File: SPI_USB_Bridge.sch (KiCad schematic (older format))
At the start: 31 parts, among them J6 USB A RECEP., Q5 IRLML2502, Q6 IRLML2502, U15 CY7C65634-28LTXC, U9 MAX3421, Y2 12MHz, Y3 12MHz

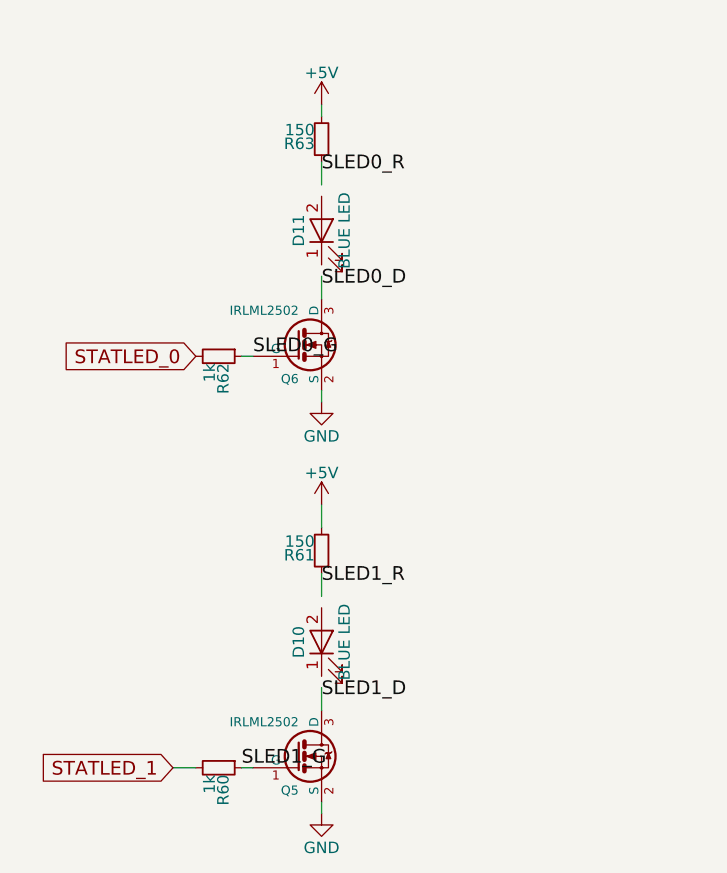
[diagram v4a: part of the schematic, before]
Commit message: Complete BOM. all resistors now 0402
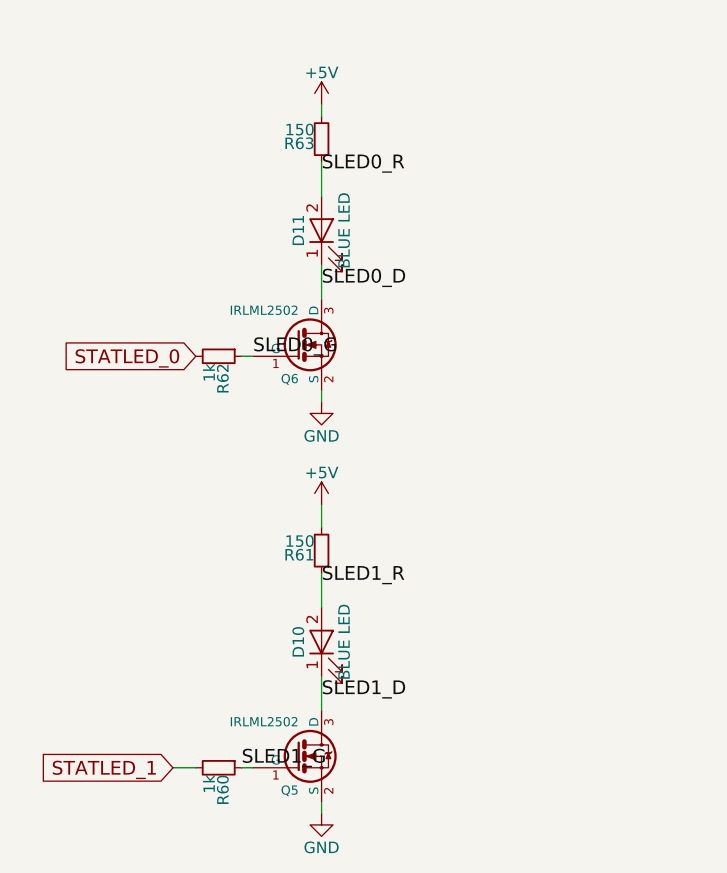
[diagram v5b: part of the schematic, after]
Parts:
- D10, D11: SPN (none) -> VLMB1300-GS08CT-ND; SPR (none) -> Digikey
- NCP1, NCP2: SPN (none) -> NCP361SNT1GOSCT-ND; SPR (none) -> Digikey
- Q5, Q6: SPN (none) -> IRLML2502PBFCT-ND; SPR (none) -> Digikey
- R100, R99: MFR Vishay Dale -> Yageo; MPN CRCW040210K0FKED -> RC0402FR-0710KL; SPN (none) -> 311-10.0KLRTR-ND; SPR (none) -> Digikey
- R101: MFR YAGEO Corporation -> Yageo; SPN (none) -> YAG3206CT-ND; SPR (none) -> Digikey
- R102, R64, R67: footprint Resistors_SMD:R_0603 -> Resistors_SMD:R_0402; MFR Vishay Dale -> Yageo; MPN CRCW060320K0FKEA -> RC0402FR-0720KL; SPN (none) -> 311-20.0KLRCT-ND; SPR (none) -> Digikey
- R60, R62: MFR Vishay Dale -> Yageo; MPN CRCW04021K00FKED -> RC0402FR-071KL; SPN (none) -> 311-1.00KLRCT-ND; SPR (none) -> Digikey
- R61, R63: MFR Vishay Dale -> Yageo; MPN CRCW0402150RFKED -> RC0402FR-07150RL; SPN (none) -> 311-150LRTR-ND; SPR (none) -> Digikey
- R65, R66: MFR Vishay Dale -> Yageo; MPN CRCW040233R0FKED -> RC0402FR-0733RL; SPN (none) -> 311-33.0LRCT-ND; SPR (none) -> Digikey
- U15: SPN (none) -> 428-3154-1-ND; SPR (none) -> Digikey
- U9: SPN (none) -> MAX3421EEHJ+TCT-ND; SPR (none) -> Digikey

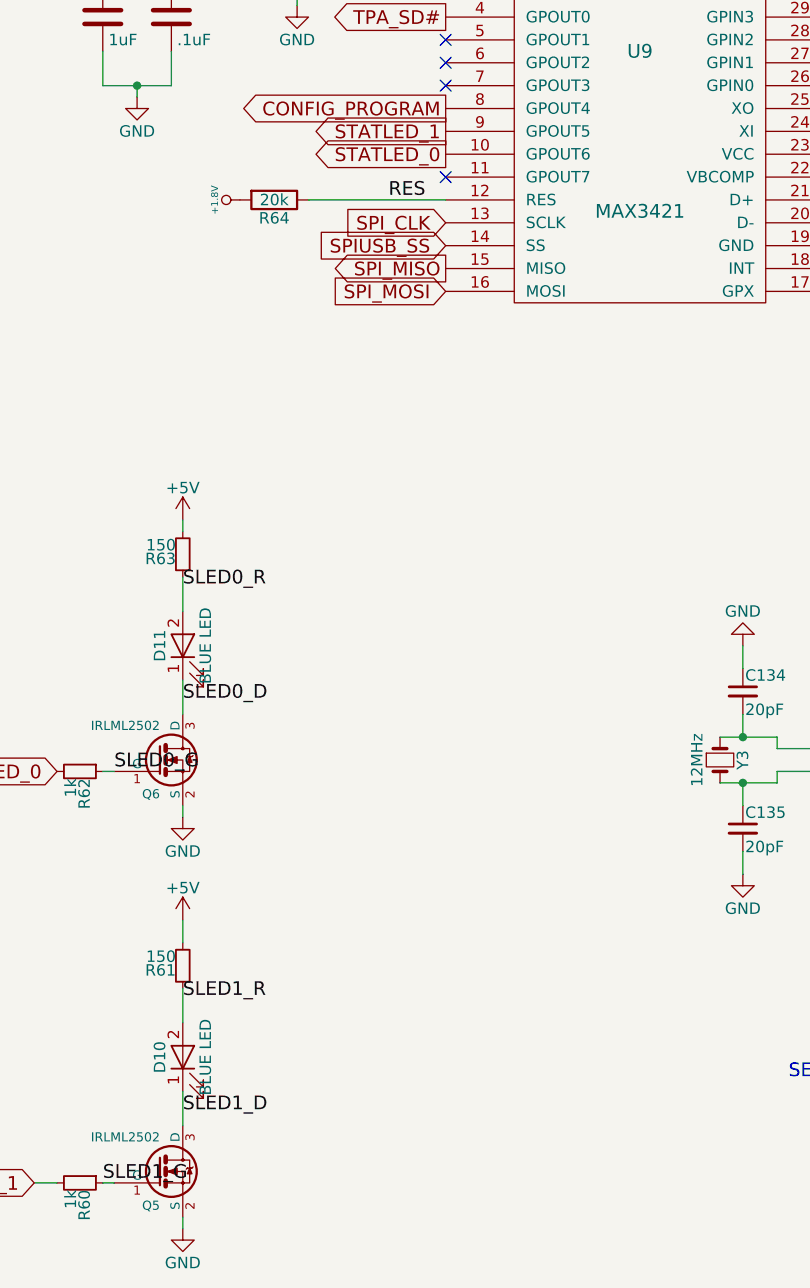
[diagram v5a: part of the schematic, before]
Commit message: added caps to audio
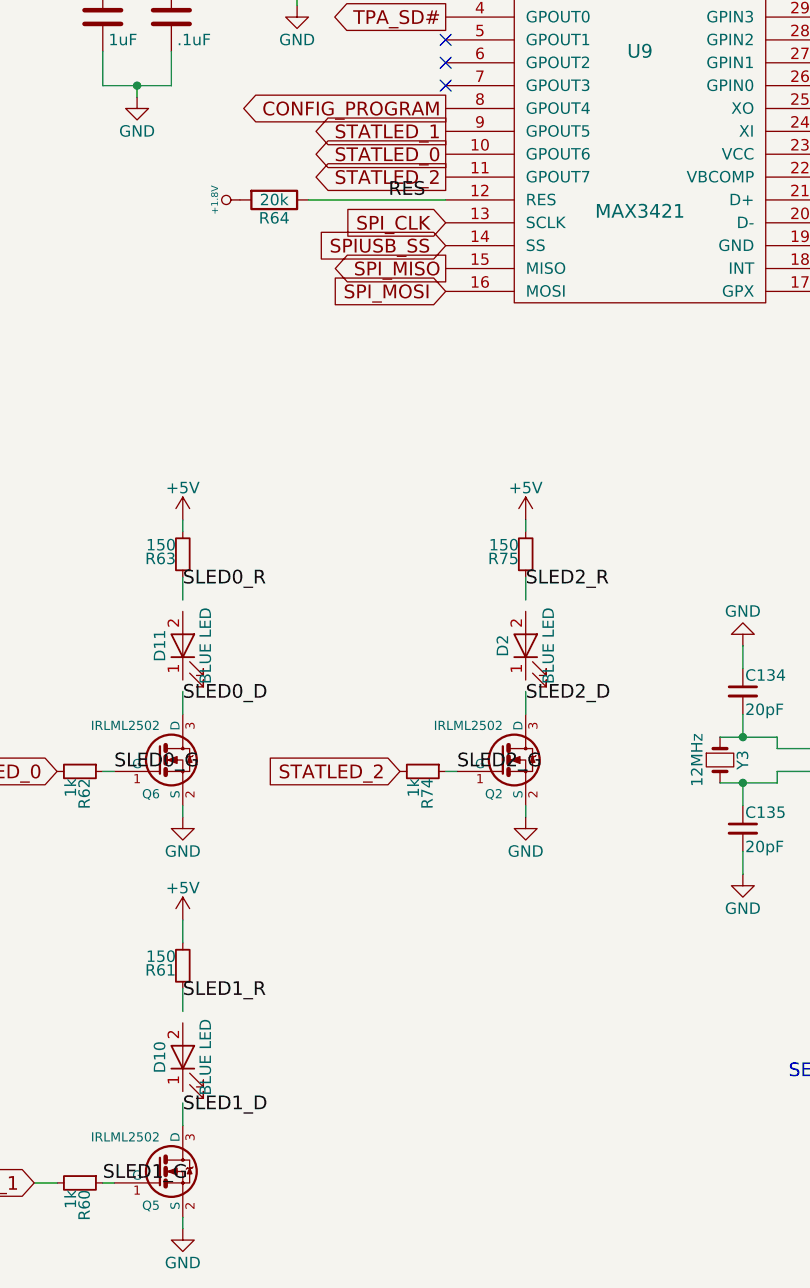
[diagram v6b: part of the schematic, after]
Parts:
- added D2: BLUE LED, LEDs:LED_0603, symbol LED
- added Q2: IRLML2502, TO_SOT_Packages_SMD:SOT-23, symbol IRLML2502
- added R74: 1k, Resistors_SMD:R_0402, symbol R_Small
- added R75: 150, Resistors_SMD:R_0402, symbol R_Small
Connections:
- net labels added: SLED2_D, SLED2_G, SLED2_R, STATLED_2
- wire segments 96 -> 101
- no-connect marks 7 -> 6

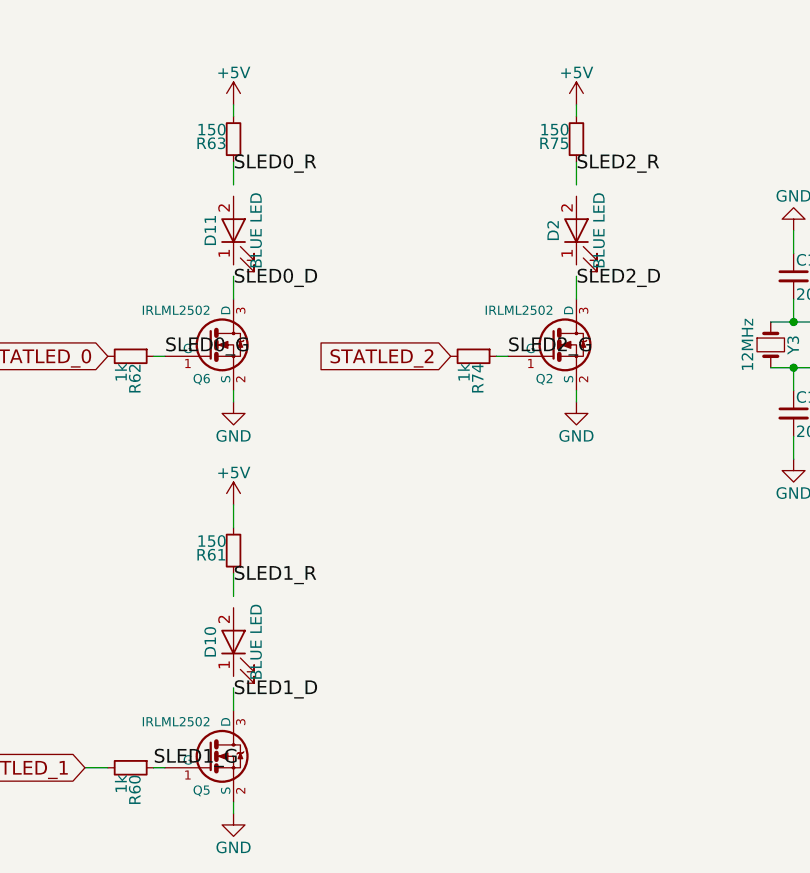
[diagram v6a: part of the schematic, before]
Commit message: about to sed replace all grounds with GND
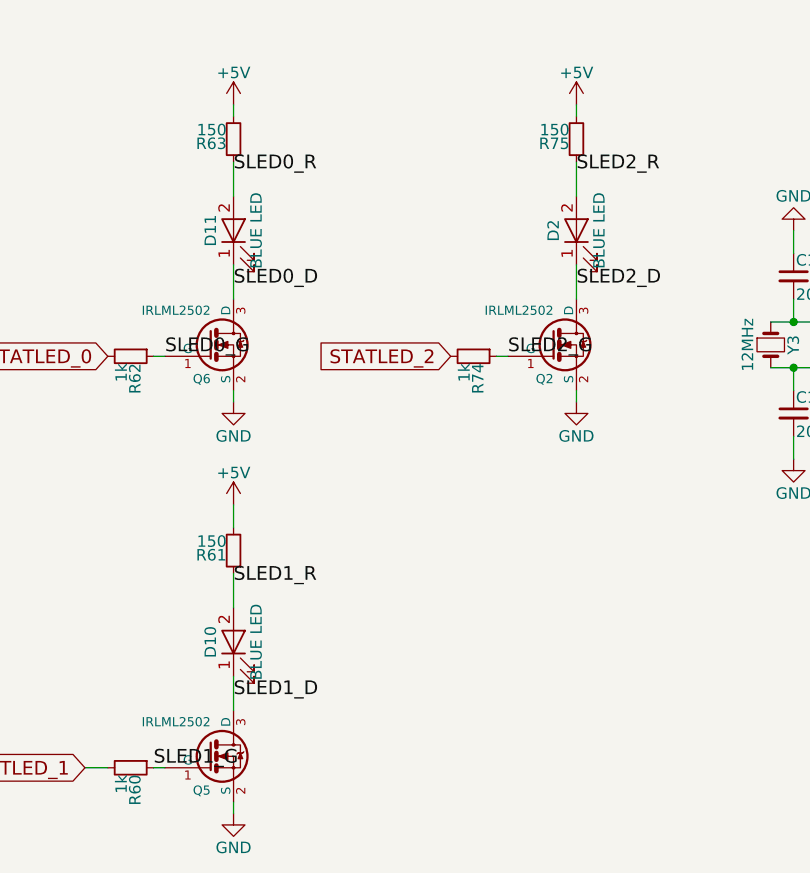
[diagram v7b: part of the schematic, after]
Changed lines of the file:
@@
 LIBS:s70fl01gs
 LIBS:PROpendous-cache
-LIBS:logo
 LIBS:JTAG
 LIBS:Audio-cache
@@
 STATLED_2
 Wire Wire Line
-	2050 6250 2050 6350
-Wire Wire Line
-	2050 6750 2050 6850
-Wire Wire Line
-	3550 4450 3550 4550
-Wire Wire Line
-	3550 4950 3550 5050
-Wire Wire Line
-	2050 4450 2050 4550
-Wire Wire Line
-	2050 4950 2050 5050
+	2050 6250 2050 6400
+Wire Wire Line
+	2050 6700 2050 6850
+Wire Wire Line
+	3550 4450 3550 4600
+Wire Wire Line
+	3550 4900 3550 5050
+Wire Wire Line
+	2050 4450 2050 4600
+Wire Wire Line
+	2050 4900 2050 5050
 $EndSCHEMATC

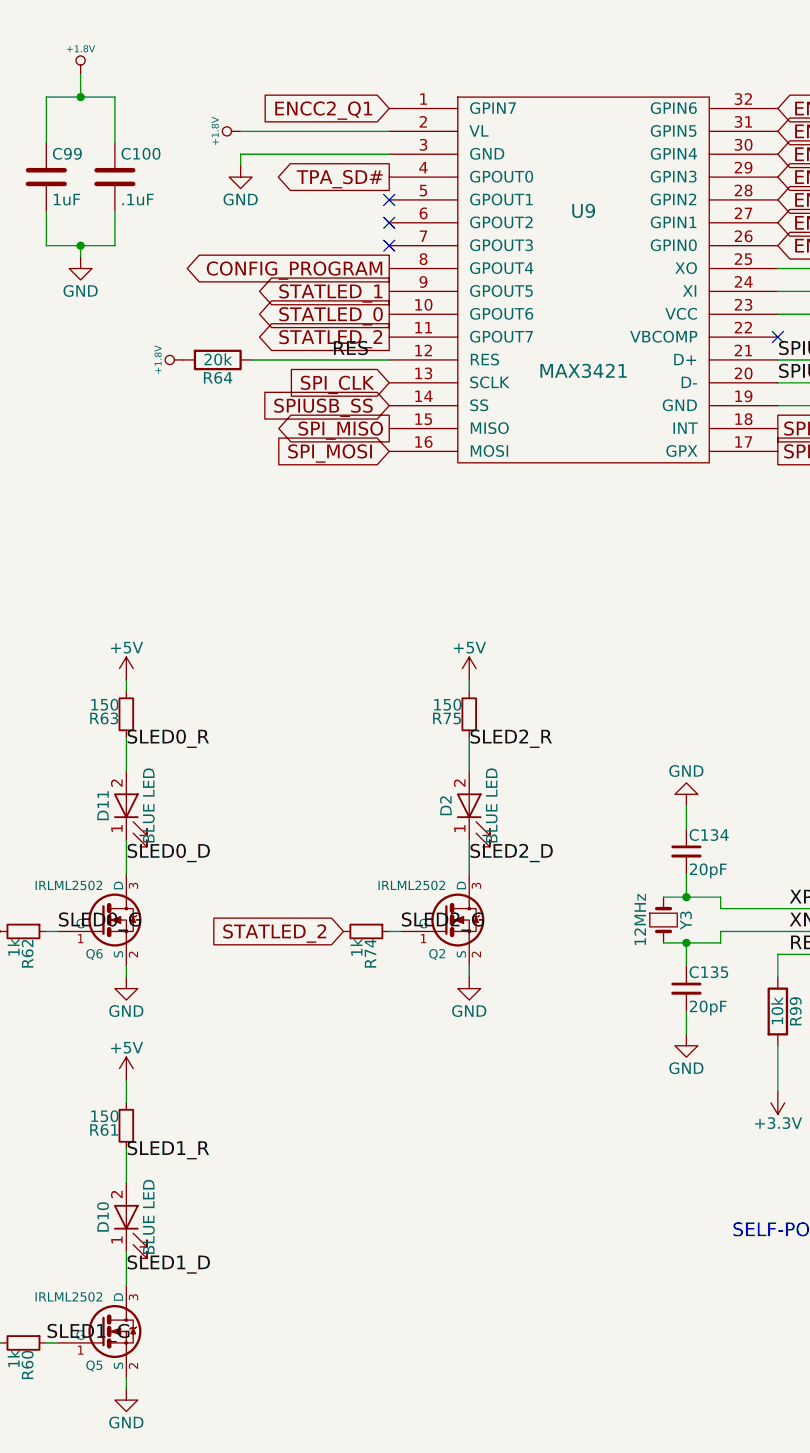
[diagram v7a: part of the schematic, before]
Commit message: about to resize all silkscreen text to 0.5
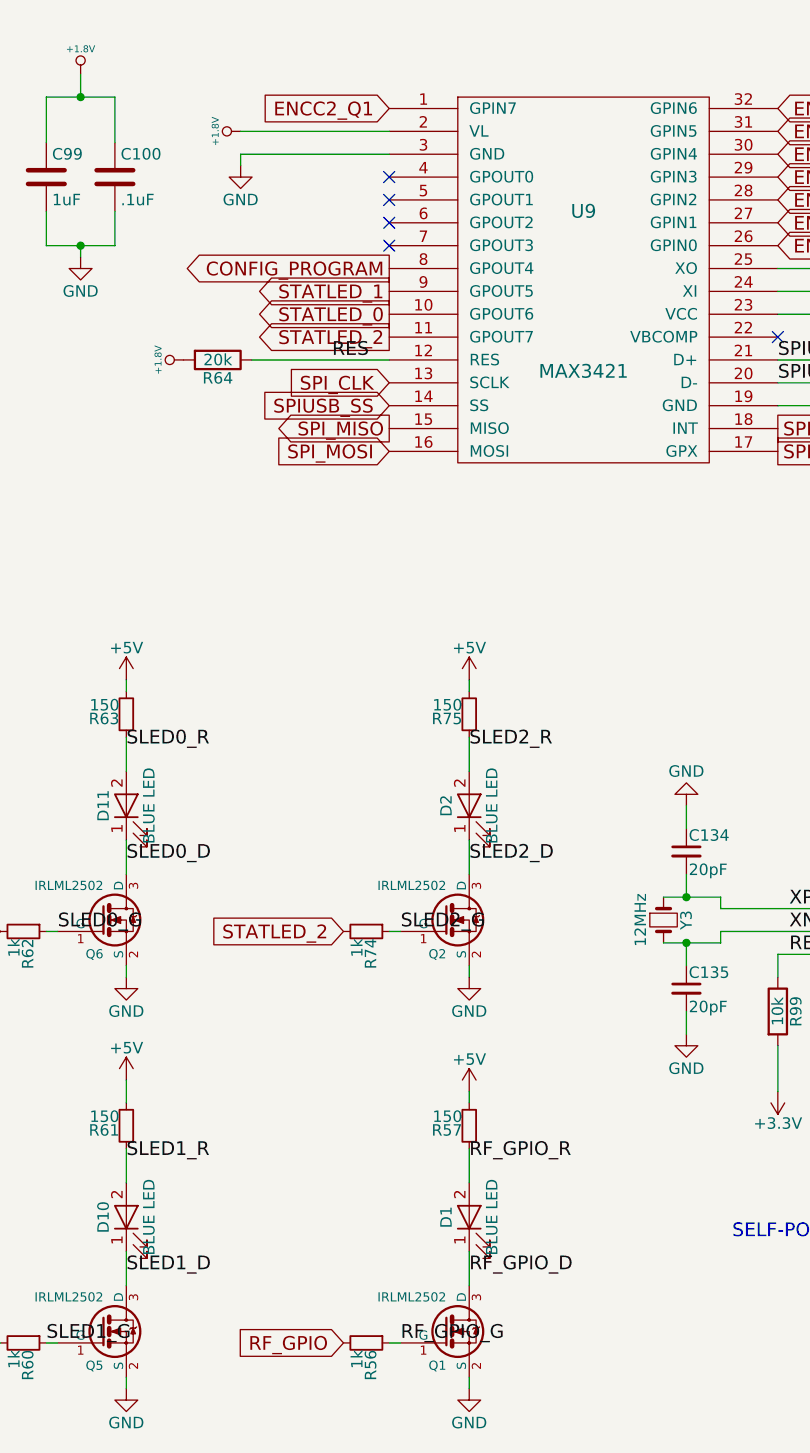
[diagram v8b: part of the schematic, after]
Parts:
- added D1: BLUE LED, LEDs:LED_0603, symbol LED
- added Q1: IRLML2502, TO_SOT_Packages_SMD:SOT-23, symbol IRLML2502
- added R56: 1k, Resistors_SMD:R_0402, symbol R_Small
- added R57: 150, Resistors_SMD:R_0402, symbol R_Small
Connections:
- net +5V: now also R57.2
- net GND: now also Q1.2 (S)
- net TPA_SD#: no longer names the net of U9.4 (GPOUT0)
- new net RF_GPIO: R56.2
- new net RF_GPIO_D: D1.1 (K), Q1.3 (D)
- new net RF_GPIO_G: Q1.1 (G), R56.1
- new net RF_GPIO_R: D1.2 (A), R57.1
- no-connect marks 6 -> 7
